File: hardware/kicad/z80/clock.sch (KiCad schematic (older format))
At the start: 1 part

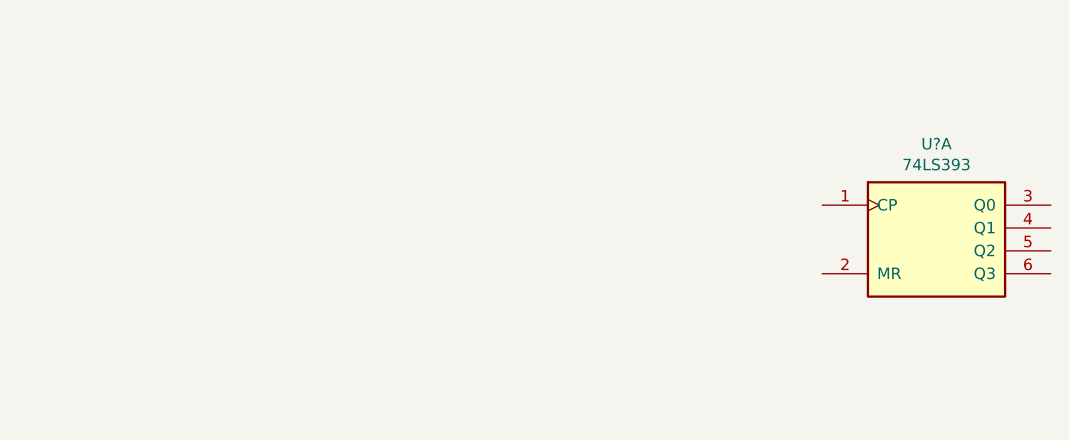
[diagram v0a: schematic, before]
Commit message: Adding more baseline schematics and notes
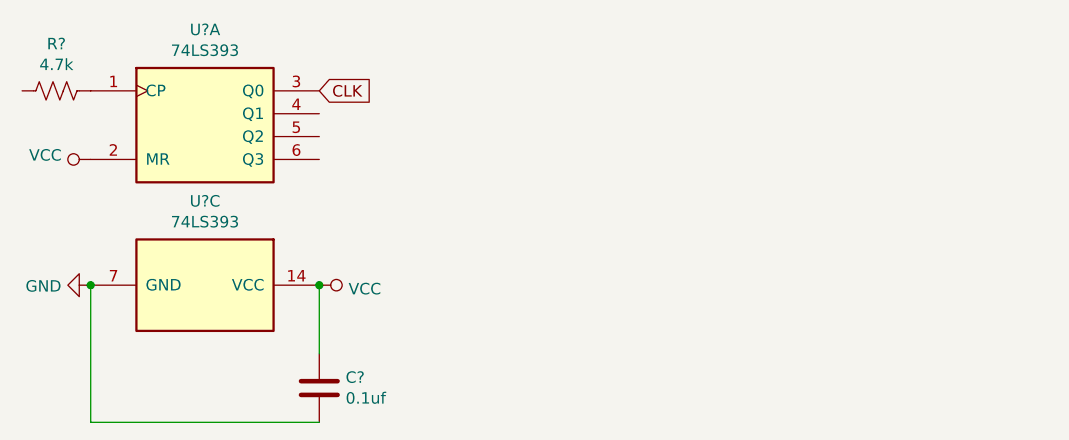
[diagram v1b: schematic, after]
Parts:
- added C?: 0.1uf, symbol Device:C
- added R?: 4.7k, symbol Device:R_US
- added U?: 74LS393, Package_DIP:DIP-14_W7.62mm_Socket, symbol 74xx:74LS393
- U?: footprint (none) -> Package_DIP:DIP-14_W7.62mm_Socket
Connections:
- net at U?.1 (CP): now also R?.2
- net VCC: now reaches U?.2 (MR)
- net VCC: now also C?.1, U?.14 (VCC)
- net CLK: now reaches U?.3 (Q0)
- new net GND: C?.2, U?.7 (GND)
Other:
- moved on the sheet: U?A
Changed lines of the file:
@@
 EESchema Schematic File Version 4
+LIBS:z80-cache
 EELAYER 26 0
 EELAYER END
 $Descr A4 11693 8268
 encoding utf-8
-Sheet 3 4
+Sheet 3 5
 Title ""
 Date ""
@@
 L 74xx:74LS393 U?
 U 1 1 66E7B2CD
-P 5650 3750
-F 0 "U?" H 5650 4117 50  0000 C CNN
-F 1 "74LS393" H 5650 4026 50  0000 C CNN
-F 2 "" H 5650 3750 50  0001 C CNN
-F 3 "74xx\\74LS393.pdf" H 5650 3750 50  0001 C CNN
-	1    5650 3750
+P 2450 3250
+F 0 "U?" H 2450 3617 50  0000 C CNN
+F 1 "74LS393" H 2450 3526 50  0000 C CNN
+F 2 "Package_DIP:DIP-14_W7.62mm_Socket" H 2450 3250 50  0001 C CNN
+F 3 "74xx\\74LS393.pdf" H 2450 3250 50  0001 C CNN
+	1    2450 3250
 	1    0    0    -1
 $EndComp
+$Comp
+L 74xx:74LS393 U?
+U 3 1 66EB3B63
+P 2450 4000
+F 0 "U?" V 2083 4000 50  0000 C CNN
+F 1 "74LS393" V 2174 4000 50  0000 C CNN
+F 2 "Package_DIP:DIP-14_W7.62mm_Socket" H 2450 4000 50  0001 C CNN
+F 3 "74xx\\74LS393.pdf" H 2450 4000 50  0001 C CNN
+	3    2450 4000
+	0    1    1    0
+$EndComp
+Text GLabel 2950 3150 2    50   Input ~ 0
+CLK
+$Comp
+L power:GND #PWR?
+U 1 1 66EB3D7E
+P 1950 4000
+F 0 "#PWR?" H 1950 3750 50  0001 C CNN
+F 1 "GND" V 1955 3872 50  0000 R CNN
+F 2 "" H 1950 4000 50  0001 C CNN
+F 3 "" H 1950 4000 50  0001 C CNN
+	1    1950 4000
+	0    1    1    0
+$EndComp
+$Comp
+L power:VCC #PWR?
+U 1 1 66EB3DB5
+P 1950 3450
+F 0 "#PWR?" H 1950 3300 50  0001 C CNN
+F 1 "VCC" V 1968 3577 50  0000 L CNN
+F 2 "" H 1950 3450 50  0001 C CNN
+F 3 "" H 1950 3450 50  0001 C CNN
+	1    1950 3450
+	0    -1   -1   0
+$EndComp
+$Comp
+L power:VCC #PWR?
+U 1 1 66EB3E0D
+P 2950 4000
+F 0 "#PWR?" H 2950 3850 50  0001 C CNN
+F 1 "VCC" V 2967 4128 50  0000 L CNN
+F 2 "" H 2950 4000 50  0001 C CNN
+F 3 "" H 2950 4000 50  0001 C CNN
+	1    2950 4000
+	0    1    1    0
+$EndComp
+$Comp
+L Device:R_US R?
+U 1 1 66EB3E55
+P 1800 3150
+F 0 "R?" V 2005 3150 50  0000 C CNN
+F 1 "4.7k" V 1914 3150 50  0000 C CNN
+F 2 "" V 1840 3140 50  0001 C CNN
+F 3 "~" H 1800 3150 50  0001 C CNN
+	1    1800 3150
+	0    -1   -1   0
+$EndComp
+$Comp
+L Device:C C?
+U 1 1 66EB3F8E
+P 2950 4450
+F 0 "C?" H 3065 4496 50  0000 L CNN
+F 1 "0.1uf" H 3065 4405 50  0000 L CNN
+F 2 "" H 2988 4300 50  0001 C CNN
+F 3 "~" H 2950 4450 50  0001 C CNN
+	1    2950 4450
+	1    0    0    -1
+$EndComp
+Wire Wire Line
+	2950 4600 1950 4600
+Wire Wire Line
+	1950 4600 1950 4000
+Connection ~ 1950 4000
+Wire Wire Line
+	2950 4300 2950 4000
+Connection ~ 2950 4000
 $EndSCHEMATC
